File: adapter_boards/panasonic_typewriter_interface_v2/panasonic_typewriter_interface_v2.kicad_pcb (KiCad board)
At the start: 2 copper layers, 57.2 x 45.5 mm, 47 parts, among them J1 KMDGX-8S-AS, J2 Conn_02x03_Odd_Even, J3 Conn_01x06_MountingPin, J4 Conn_01x08_MountingPin, J5 Conn_01x04_MountingPin, J6 Conn_01x09_Socket, J7 Conn_01x09_Socket, J8 Conn_01x10_Pin, SW1 SW_SPDT, SW2 SW_Push

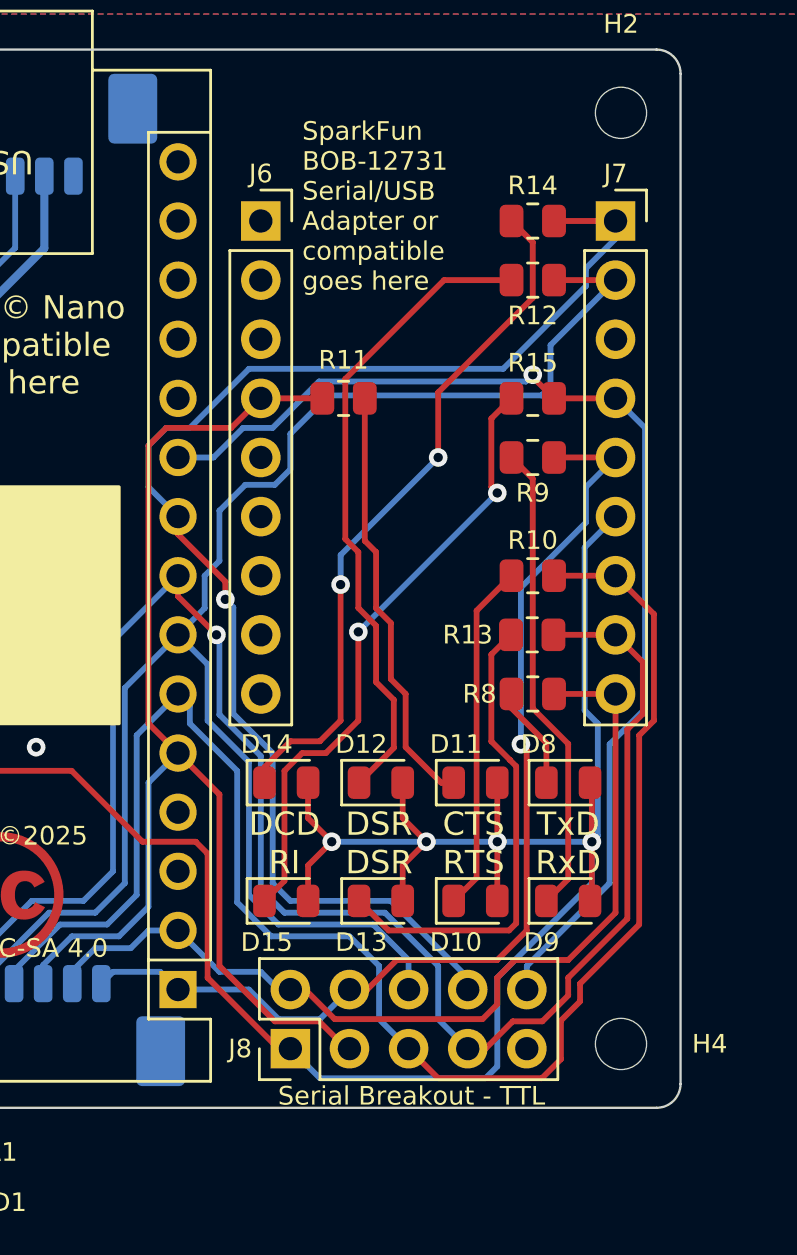
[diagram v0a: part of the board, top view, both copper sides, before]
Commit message: adjust position of serial module
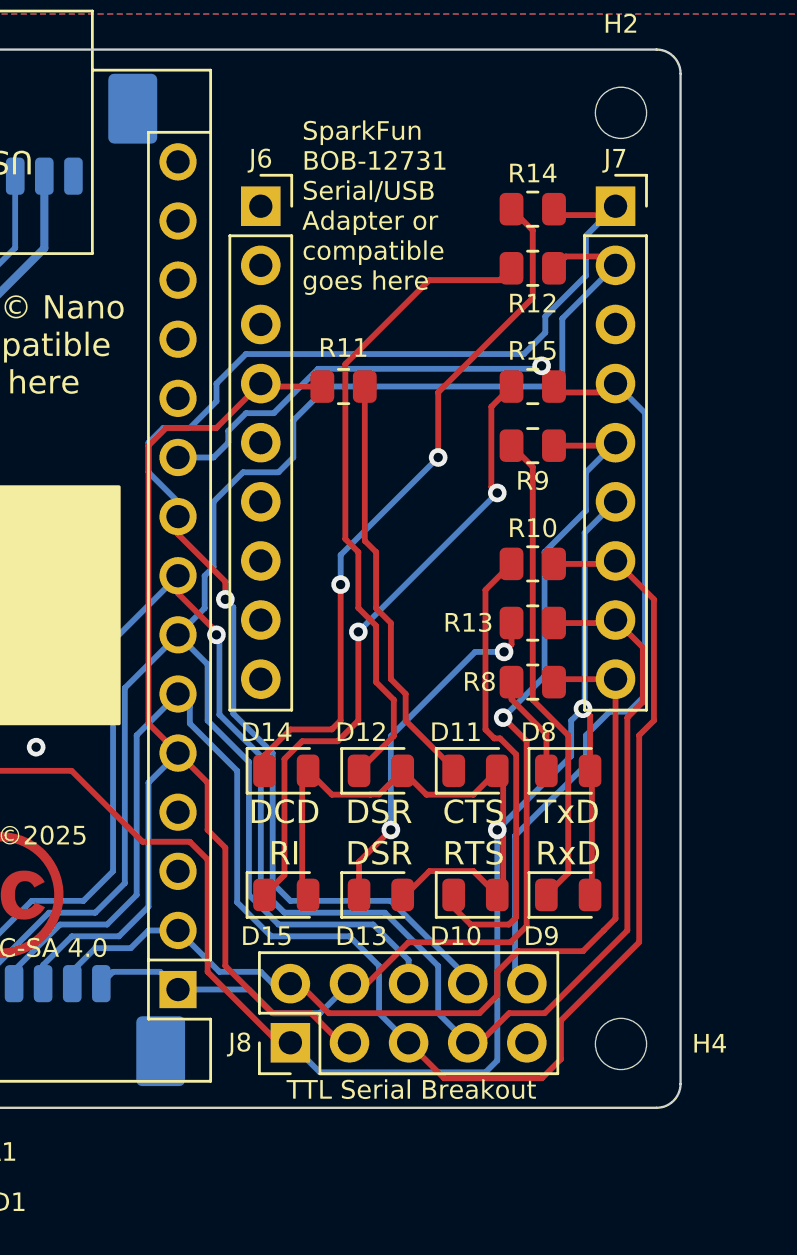
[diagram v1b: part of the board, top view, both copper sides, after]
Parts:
- moved J6 0.63 mm to (156.0, 73.0)
- moved J7 0.63 mm to (171.2, 73.0)
- moved R13 0.51 mm to (167.6, 90.9)
- moved D11 0.51 mm to (165.2, 97.3)
- moved D12 0.51 mm to (161.1, 97.3)
- moved D14 0.51 mm to (157.1, 97.3)
- moved D8 0.51 mm to (169.2, 97.3)
- moved R10 0.51 mm to (167.6, 88.4)
- moved R12 0.51 mm to (167.6, 75.7)
- moved R8 0.51 mm to (167.6, 93.5)
- moved R11 0.51 mm to (159.5, 80.8)
- moved R14 0.51 mm to (167.6, 73.2)
- moved R15 0.51 mm to (167.6, 80.8)
- moved R9 0.51 mm to (167.6, 83.3)
- moved D10 0.25 mm to (165.2, 102.6)
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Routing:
- net Net-(D13-K): track 20.6 -> 15.5 mm, vias 0 -> 2
- net Net-(D10-K): track 15.0 -> 20.0 mm
- net OUTPUT_RI: track 48.8 -> 50.9 mm
- net SERIAL_VCCIO: track 174.9 -> 176.6 mm, vias 5 -> 3
- net OUTPUT_DCD: track 59.2 -> 60.5 mm
- net OUTPUT_DSR: track 72.8 -> 73.9 mm
- net SERIAL0_TX: track 45.7 -> 46.7 mm
- net SERIAL0_RX: track 40.2 -> 40.8 mm
- net Net-(D15-K): track 26.8 -> 27.3 mm
- net INPUT_RTS: track 70.5 -> 71.0 mm
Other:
- board text added: "TTL Serial Breakout"
- board text removed: "Serial Breakout - TTL"

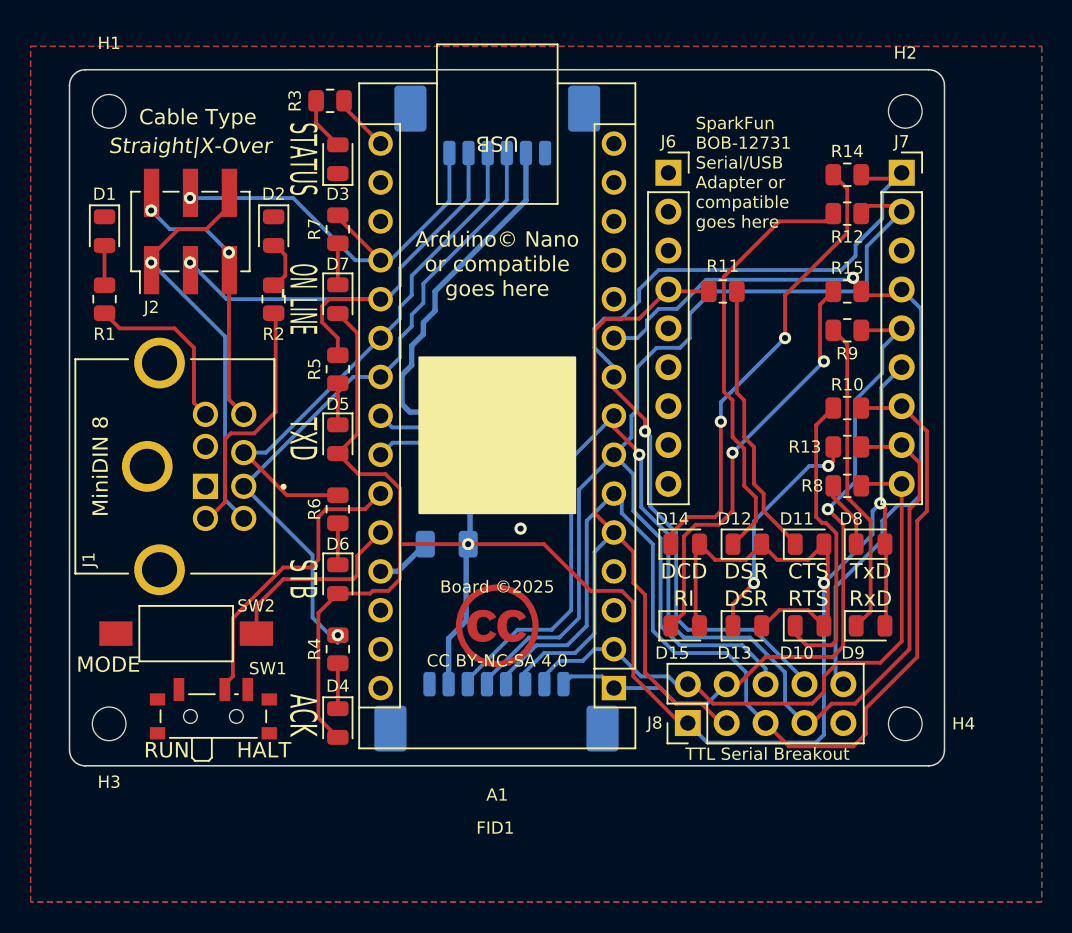
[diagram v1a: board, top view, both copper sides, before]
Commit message: Added DE-9 connector
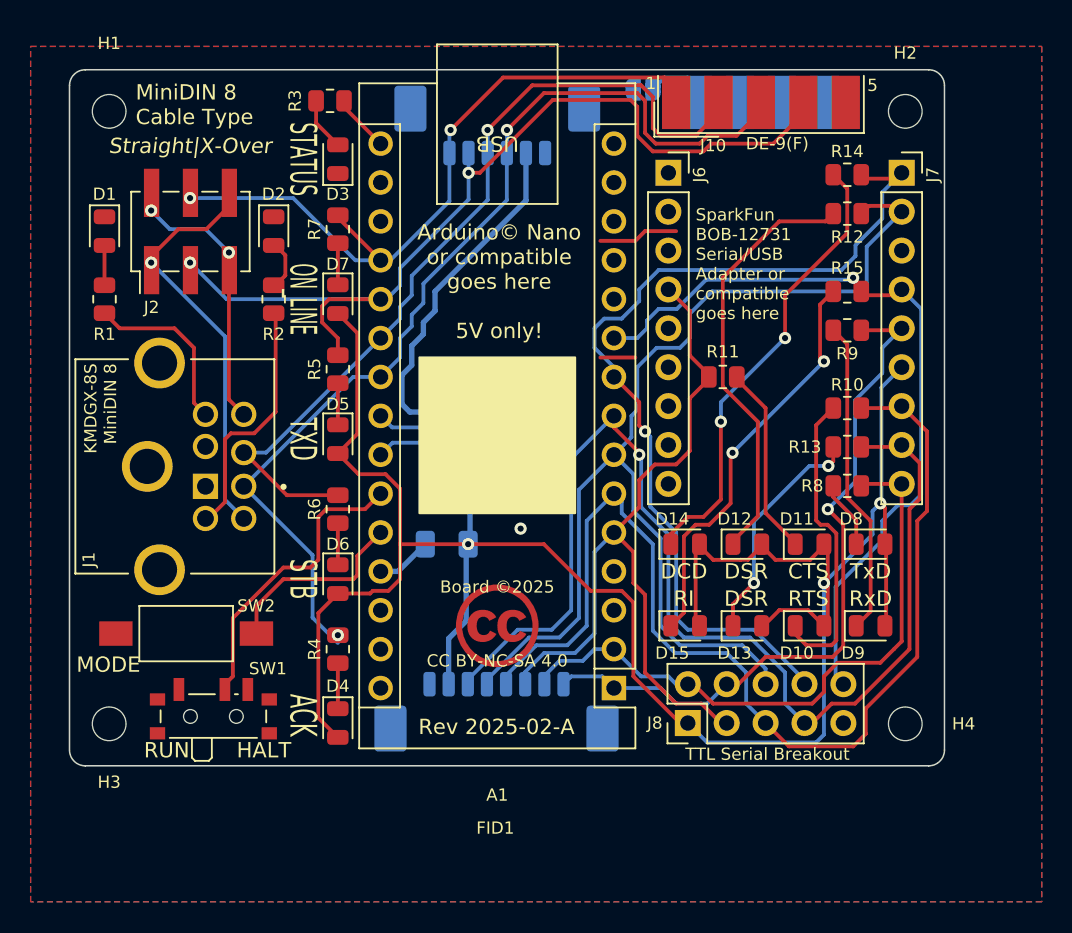
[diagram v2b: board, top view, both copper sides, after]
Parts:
- added J10: Conn_01x09, Connector_Dsub:DSUB-9_Female_EdgeMount_P2.77mm, F.Cu at (162.0, 68.4)
- added JP1: Jumper_2_Bridged, Jumper:SolderJumper-2_P1.3mm_Open_RoundedPad1.0x1.5mm, B.Cu at (154.3, 67.6)
- moved R11 5.59 mm to (159.5, 86.4)
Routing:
- net TXD: track 32.8 -> 60.9 mm, vias 1 -> 2
- net ~{ACK}: track 42.7 -> 65.9 mm, vias 1 -> 2
- net ~{STB}: track 33.8 -> 55.4 mm, vias 0 -> 1
- net ~{ON_LINE}: track 26.8 -> 45.7 mm, vias 1 -> 2
- net GND: track 0.00 -> 7.50 mm
- net Net-(D11-K): track 18.1 -> 12.5 mm
- net Net-(J10-Pin_6): track 0.00 -> 4.48 mm
- net OUTPUT_CTS: track 52.4 -> 50.5 mm
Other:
- board text added: "9"
- board text added: "Arduino© Nano or compatible goes here 5V only!"
- board text added: "DE-9(F)"
- board text added: "DE-9(F) to RK/KX typewriters"
- board text added: "KMDGX-8S MiniDIN 8"
- board text added: "MiniDIN 8 Cable Type"
- board text added: "MiniDIn-8 to KX-R typewriters"
- board text removed: "Arduino© Nano or compatible goes here"
- board text removed: "Cable Type"
- board text removed: "MiniDIN 8"
